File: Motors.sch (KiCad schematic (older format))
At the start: 12 parts

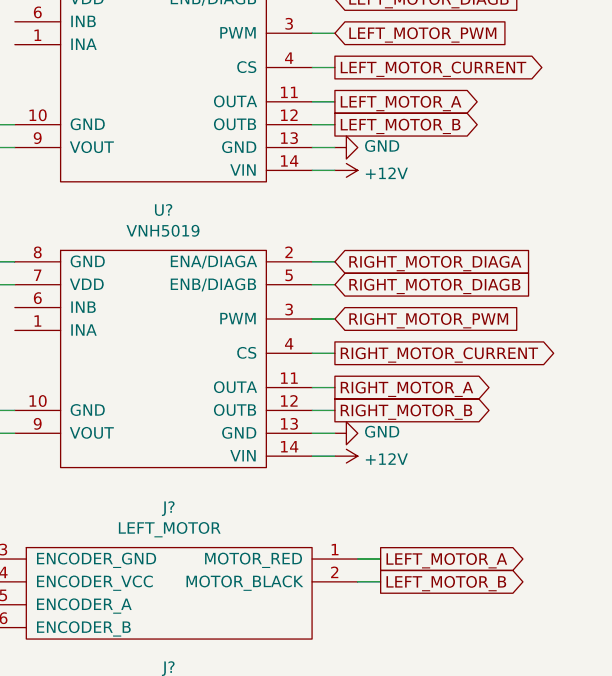
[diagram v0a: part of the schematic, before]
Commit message: Added fuses
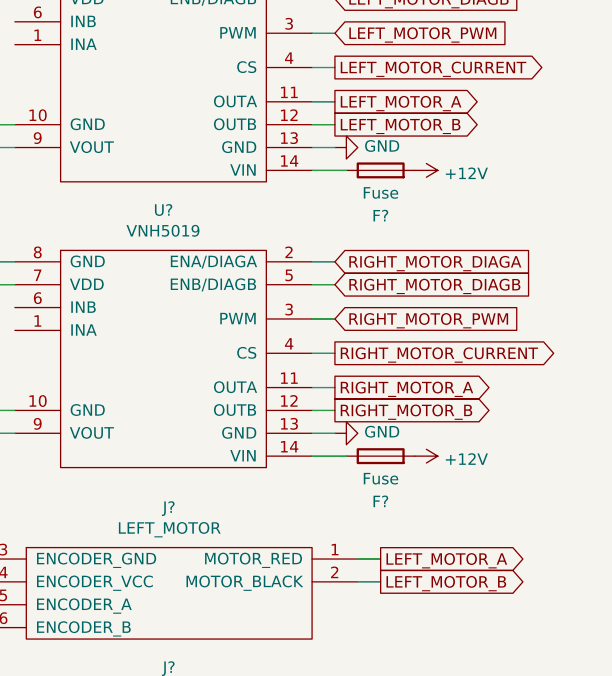
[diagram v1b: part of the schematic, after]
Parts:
- added F? (x2): Fuse, symbol Device:Fuse
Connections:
- net +12V: now also F?.2, F?.2; no longer U?.14 (VIN), U?.14 (VIN)
- new net: F?.1, U?.14 (VIN) (x2)
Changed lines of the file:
@@
 	6900 2300 7000 2300
-Wire Wire Line
-	6900 2400 7000 2400
 Wire Wire Line
 	5600 1550 5500 1550
@@
 L power:+12V #PWR?
 U 1 1 5E0DA565
-P 7000 3650
+P 7350 3650
 AR Path="/5E0DA565" Ref="#PWR?"  Part="1"
 AR Path="/5E0C61A9/5E0DA565" Ref="#PWR?"  Part="1"
-F 0 "#PWR?" H 7000 3500 50  0001 C CNN
-F 1 "+12V" V 7015 3778 50  0000 L CNN
-F 2 "" H 7000 3650 50  0001 C CNN
-F 3 "" H 7000 3650 50  0001 C CNN
-	1    7000 3650
+F 0 "#PWR?" H 7350 3500 50  0001 C CNN
+F 1 "+12V" V 7365 3778 50  0000 L CNN
+F 2 "" H 7350 3650 50  0001 C CNN
+F 3 "" H 7350 3650 50  0001 C CNN
+	1    7350 3650
 	0    1    1    0
 $EndComp
@@
 	6900 3550 7000 3550
 Wire Wire Line
-	6900 3650 7000 3650
-Wire Wire Line
 	5600 2800 5500 2800
 Wire Wire Line
@@
 L power:+12V #PWR?
 U 1 1 5E0DA62B
-P 7000 2400
+P 7350 2400
 AR Path="/5E0DA62B" Ref="#PWR?"  Part="1"
 AR Path="/5E0C61A9/5E0DA62B" Ref="#PWR?"  Part="1"
-F 0 "#PWR?" H 7000 2250 50  0001 C CNN
-F 1 "+12V" V 7015 2528 50  0000 L CNN
-F 2 "" H 7000 2400 50  0001 C CNN
-F 3 "" H 7000 2400 50  0001 C CNN
-	1    7000 2400
-	0    1    1    0
-$EndComp
+F 0 "#PWR?" H 7350 2250 50  0001 C CNN
+F 1 "+12V" V 7365 2528 50  0000 L CNN
+F 2 "" H 7350 2400 50  0001 C CNN
+F 3 "" H 7350 2400 50  0001 C CNN
+	1    7350 2400
+	0    1    1    0
+$EndComp
+$Comp
+L Device:Fuse F?
+U 1 1 5E2BC2E8
+P 7200 3650
+F 0 "F?" V 7000 3650 50  0000 C CNN
+F 1 "Fuse" V 7100 3650 50  0000 C CNN
+F 2 "" V 7130 3650 50  0001 C CNN
+F 3 "~" H 7200 3650 50  0001 C CNN
+	1    7200 3650
+	0    -1   -1   0
+$EndComp
+Wire Wire Line
+	6900 3650 7050 3650
+$Comp
+L Device:Fuse F?
+U 1 1 5E2BEBB4
+P 7200 2400
+F 0 "F?" V 7000 2400 50  0000 C CNN
+F 1 "Fuse" V 7100 2400 50  0000 C CNN
+F 2 "" V 7130 2400 50  0001 C CNN
+F 3 "~" H 7200 2400 50  0001 C CNN
+	1    7200 2400
+	0    -1   -1   0
+$EndComp
+Wire Wire Line
+	6900 2400 7050 2400
 $EndSCHEMATC

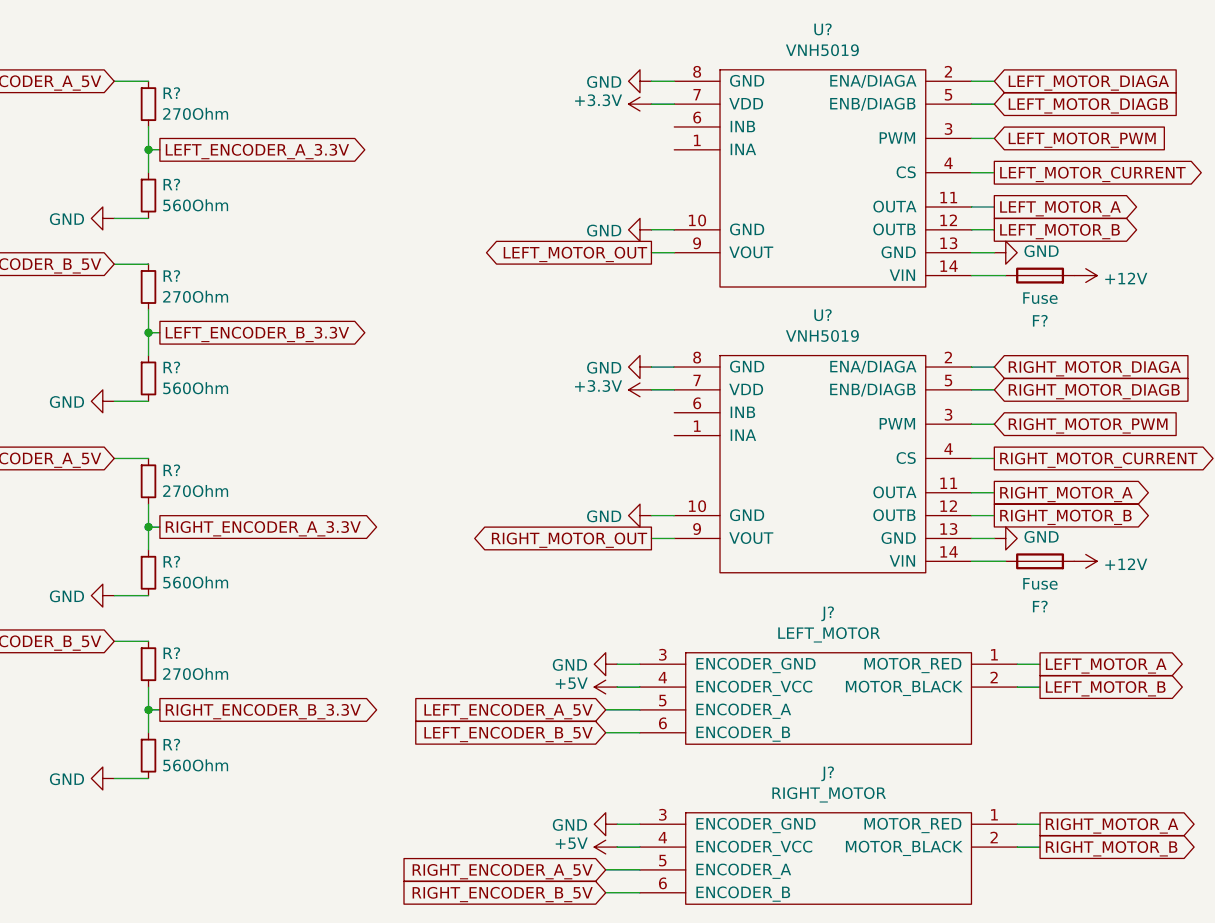
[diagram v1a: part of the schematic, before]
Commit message: Added footprints
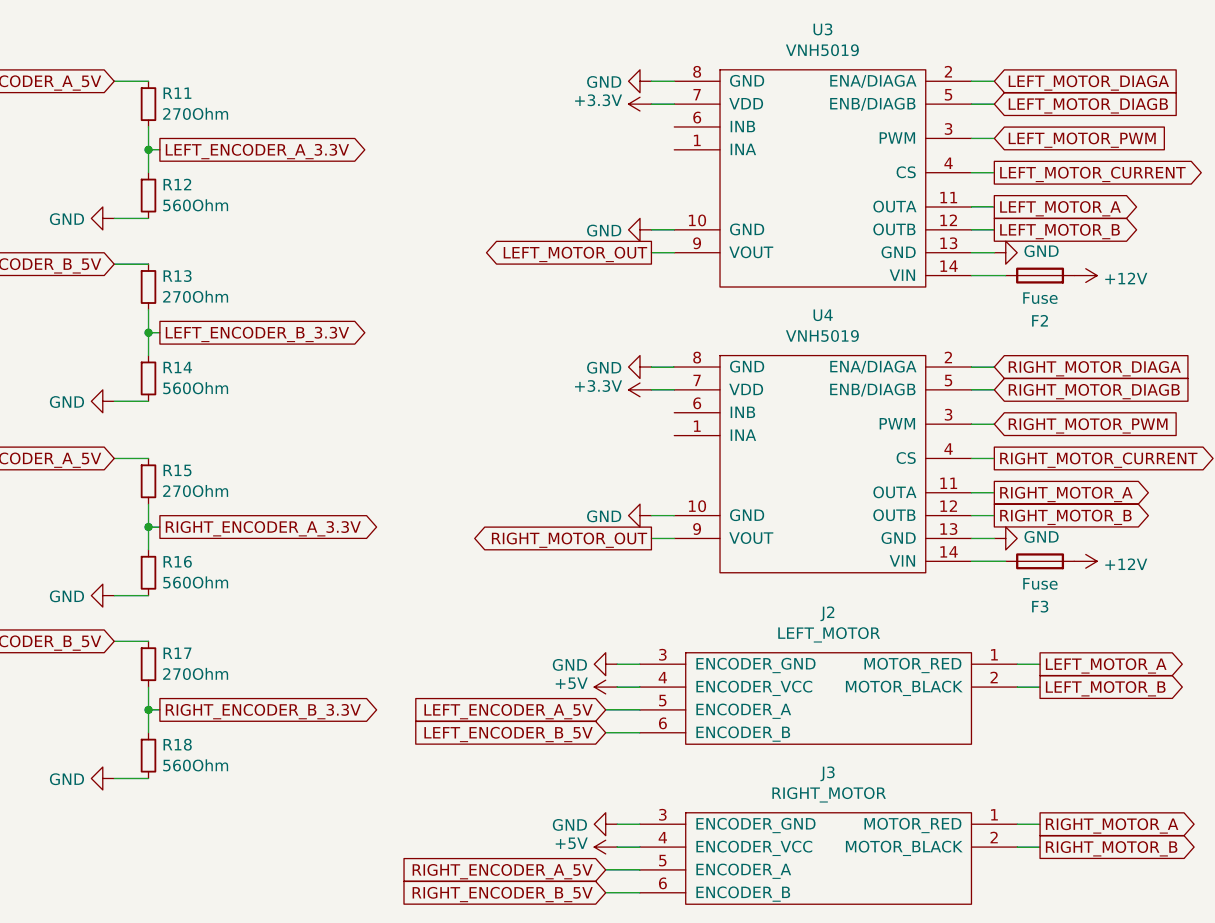
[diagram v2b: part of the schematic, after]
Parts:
- gave numbers to parts that had none: 14
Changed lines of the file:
@@
 P 6200 2500
 AR Path="/5E0DA51C" Ref="U?"  Part="1"
-AR Path="/5E0C61A9/5E0DA51C" Ref="U?"  Part="1"
-F 0 "U?" H 6250 3675 50  0000 C CNN
+AR Path="/5E0C61A9/5E0DA51C" Ref="U3"  Part="1"
+F 0 "U3" H 6250 3675 50  0000 C CNN
 F 1 "VNH5019" H 6250 3584 50  0000 C CNN
 F 2 "" H 6200 2500 50  0001 C CNN
@@
 P 5500 1550
 AR Path="/5E0DA522" Ref="#PWR?"  Part="1"
-AR Path="/5E0C61A9/5E0DA522" Ref="#PWR?"  Part="1"
-F 0 "#PWR?" H 5500 1300 50  0001 C CNN
+AR Path="/5E0C61A9/5E0DA522" Ref="#PWR0131"  Part="1"
+F 0 "#PWR0131" H 5500 1300 50  0001 C CNN
 F 1 "GND" V 5505 1422 50  0000 R CNN
 F 2 "" H 5500 1550 50  0001 C CNN
@@
 P 5500 2200
 AR Path="/5E0DA528" Ref="#PWR?"  Part="1"
-AR Path="/5E0C61A9/5E0DA528" Ref="#PWR?"  Part="1"
-F 0 "#PWR?" H 5500 1950 50  0001 C CNN
+AR Path="/5E0C61A9/5E0DA528" Ref="#PWR0132"  Part="1"
+F 0 "#PWR0132" H 5500 1950 50  0001 C CNN
 F 1 "GND" V 5505 2072 50  0000 R CNN
 F 2 "" H 5500 2200 50  0001 C CNN
@@
 P 5500 1650
 AR Path="/5E0DA52E" Ref="#PWR?"  Part="1"
-AR Path="/5E0C61A9/5E0DA52E" Ref="#PWR?"  Part="1"
-F 0 "#PWR?" H 5500 1500 50  0001 C CNN
+AR Path="/5E0C61A9/5E0DA52E" Ref="#PWR0133"  Part="1"
+F 0 "#PWR0133" H 5500 1500 50  0001 C CNN
 F 1 "+3.3V" V 5515 1778 50  0000 L CNN
 F 2 "" H 5500 1650 50  0001 C CNN
@@
 P 7000 2300
 AR Path="/5E0DA534" Ref="#PWR?"  Part="1"
-AR Path="/5E0C61A9/5E0DA534" Ref="#PWR?"  Part="1"
-F 0 "#PWR?" H 7000 2050 50  0001 C CNN
+AR Path="/5E0C61A9/5E0DA534" Ref="#PWR0134"  Part="1"
+F 0 "#PWR0134" H 7000 2050 50  0001 C CNN
 F 1 "GND" V 7005 2172 50  0000 R CNN
 F 2 "" H 7000 2300 50  0001 C CNN
@@
 P 6200 3750
 AR Path="/5E0DA54D" Ref="U?"  Part="1"
-AR Path="/5E0C61A9/5E0DA54D" Ref="U?"  Part="1"
-F 0 "U?" H 6250 4925 50  0000 C CNN
+AR Path="/5E0C61A9/5E0DA54D" Ref="U4"  Part="1"
+F 0 "U4" H 6250 4925 50  0000 C CNN
 F 1 "VNH5019" H 6250 4834 50  0000 C CNN
 F 2 "" H 6200 3750 50  0001 C CNN
@@
 P 5500 2800
 AR Path="/5E0DA553" Ref="#PWR?"  Part="1"
-AR Path="/5E0C61A9/5E0DA553" Ref="#PWR?"  Part="1"
-F 0 "#PWR?" H 5500 2550 50  0001 C CNN
+AR Path="/5E0C61A9/5E0DA553" Ref="#PWR0135"  Part="1"
+F 0 "#PWR0135" H 5500 2550 50  0001 C CNN
 F 1 "GND" V 5505 2672 50  0000 R CNN
 F 2 "" H 5500 2800 50  0001 C CNN
@@
 P 5500 3450
 AR Path="/5E0DA559" Ref="#PWR?"  Part="1"
-AR Path="/5E0C61A9/5E0DA559" Ref="#PWR?"  Part="1"
-F 0 "#PWR?" H 5500 3200 50  0001 C CNN
+AR Path="/5E0C61A9/5E0DA559" Ref="#PWR0136"  Part="1"
+F 0 "#PWR0136" H 5500 3200 50  0001 C CNN
 F 1 "GND" V 5505 3322 50  0000 R CNN
 F 2 "" H 5500 3450 50  0001 C CNN
@@
 P 5500 2900
 AR Path="/5E0DA55F" Ref="#PWR?"  Part="1"
-AR Path="/5E0C61A9/5E0DA55F" Ref="#PWR?"  Part="1"
-F 0 "#PWR?" H 5500 2750 50  0001 C CNN
+AR Path="/5E0C61A9/5E0DA55F" Ref="#PWR0137"  Part="1"
+F 0 "#PWR0137" H 5500 2750 50  0001 C CNN
 F 1 "+3.3V" V 5515 3028 50  0000 L CNN
 F 2 "" H 5500 2900 50  0001 C CNN
@@
 P 7350 3650
 AR Path="/5E0DA565" Ref="#PWR?"  Part="1"
-AR Path="/5E0C61A9/5E0DA565" Ref="#PWR?"  Part="1"
-F 0 "#PWR?" H 7350 3500 50  0001 C CNN
+AR Path="/5E0C61A9/5E0DA565" Ref="#PWR0138"  Part="1"
+F 0 "#PWR0138" H 7350 3500 50  0001 C CNN
 F 1 "+12V" V 7365 3778 50  0000 L CNN
 F 2 "" H 7350 3650 50  0001 C CNN
@@
 P 7000 3550
 AR Path="/5E0DA56B" Ref="#PWR?"  Part="1"
-AR Path="/5E0C61A9/5E0DA56B" Ref="#PWR?"  Part="1"
-F 0 "#PWR?" H 7000 3300 50  0001 C CNN
+AR Path="/5E0C61A9/5E0DA56B" Ref="#PWR0139"  Part="1"
+F 0 "#PWR0139" H 7000 3300 50  0001 C CNN
 F 1 "GND" V 7005 3422 50  0000 R CNN
 F 2 "" H 7000 3550 50  0001 C CNN
@@
 P 6300 4550
 AR Path="/5E0DA584" Ref="J?"  Part="1"
-AR Path="/5E0C61A9/5E0DA584" Ref="J?"  Part="1"
-F 0 "J?" H 6275 5225 50  0000 C CNN
+AR Path="/5E0C61A9/5E0DA584" Ref="J2"  Part="1"
+F 0 "J2" H 6275 5225 50  0000 C CNN
 F 1 "LEFT_MOTOR" H 6275 5134 50  0000 C CNN
 F 2 "" H 6300 4550 50  0001 C CNN
@@
 P 6300 5250
 AR Path="/5E0DA58A" Ref="J?"  Part="1"
-AR Path="/5E0C61A9/5E0DA58A" Ref="J?"  Part="1"
-F 0 "J?" H 6275 5925 50  0000 C CNN
+AR Path="/5E0C61A9/5E0DA58A" Ref="J3"  Part="1"
+F 0 "J3" H 6275 5925 50  0000 C CNN
 F 1 "RIGHT_MOTOR" H 6275 5834 50  0000 C CNN
 F 2 "" H 6300 5250 50  0001 C CNN
@@
 P 5350 4100
 AR Path="/5E0DA594" Ref="#PWR?"  Part="1"
-AR Path="/5E0C61A9/5E0DA594" Ref="#PWR?"  Part="1"
-F 0 "#PWR?" H 5350 3850 50  0001 C CNN
+AR Path="/5E0C61A9/5E0DA594" Ref="#PWR0140"  Part="1"
+F 0 "#PWR0140" H 5350 3850 50  0001 C CNN
 F 1 "GND" V 5355 3972 50  0000 R CNN
 F 2 "" H 5350 4100 50  0001 C CNN
@@
 P 5350 4800
 AR Path="/5E0DA59A" Ref="#PWR?"  Part="1"
-AR Path="/5E0C61A9/5E0DA59A" Ref="#PWR?"  Part="1"
-F 0 "#PWR?" H 5350 4550 50  0001 C CNN
+AR Path="/5E0C61A9/5E0DA59A" Ref="#PWR0141"  Part="1"
+F 0 "#PWR0141" H 5350 4550 50  0001 C CNN
 F 1 "GND" V 5355 4672 50  0000 R CNN
 F 2 "" H 5350 4800 50  0001 C CNN
@@
 P 5350 4200
 AR Path="/5E0DA5A0" Ref="#PWR?"  Part="1"
-AR Path="/5E0C61A9/5E0DA5A0" Ref="#PWR?"  Part="1"
-F 0 "#PWR?" H 5350 4050 50  0001 C CNN
+AR Path="/5E0C61A9/5E0DA5A0" Ref="#PWR0142"  Part="1"
+F 0 "#PWR0142" H 5350 4050 50  0001 C CNN
 F 1 "+5V" V 5365 4328 50  0000 L CNN
 F 2 "" H 5350 4200 50  0001 C CNN
@@
 P 5350 4900
 AR Path="/5E0DA5A6" Ref="#PWR?"  Part="1"
-AR Path="/5E0C61A9/5E0DA5A6" Ref="#PWR?"  Part="1"
-F 0 "#PWR?" H 5350 4750 50  0001 C CNN
+AR Path="/5E0C61A9/5E0DA5A6" Ref="#PWR0143"  Part="1"
+F 0 "#PWR0143" H 5350 4750 50  0001 C CNN
 F 1 "+5V" V 5365 5028 50  0000 L CNN
 F 2 "" H 5350 4900 50  0001 C CNN
@@
 P 3300 1650
 AR Path="/5E0DA5BD" Ref="R?"  Part="1"
-AR Path="/5E0C61A9/5E0DA5BD" Ref="R?"  Part="1"
-F 0 "R?" H 3359 1696 50  0000 L CNN
+AR Path="/5E0C61A9/5E0DA5BD" Ref="R11"  Part="1"
+F 0 "R11" H 3359 1696 50  0000 L CNN
 F 1 "270Ohm" H 3359 1605 50  0000 L CNN
 F 2 "" H 3300 1650 50  0001 C CNN
@@
 P 3300 2050
 AR Path="/5E0DA5C3" Ref="R?"  Part="1"
-AR Path="/5E0C61A9/5E0DA5C3" Ref="R?"  Part="1"
-F 0 "R?" H 3359 2096 50  0000 L CNN
+AR Path="/5E0C61A9/5E0DA5C3" Ref="R12"  Part="1"
+F 0 "R12" H 3359 2096 50  0000 L CNN
 F 1 "560Ohm" H 3359 2005 50  0000 L CNN
 F 2 "" H 3300 2050 50  0001 C CNN
@@
 P 3150 2150
 AR Path="/5E0DA5C9" Ref="#PWR?"  Part="1"
-AR Path="/5E0C61A9/5E0DA5C9" Ref="#PWR?"  Part="1"
-F 0 "#PWR?" H 3150 1900 50  0001 C CNN
+AR Path="/5E0C61A9/5E0DA5C9" Ref="#PWR0144"  Part="1"
+F 0 "#PWR0144" H 3150 1900 50  0001 C CNN
 F 1 "GND" V 3155 2022 50  0000 R CNN
 F 2 "" H 3150 2150 50  0001 C CNN
@@
 P 3300 2450
 AR Path="/5E0DA5D7" Ref="R?"  Part="1"
-AR Path="/5E0C61A9/5E0DA5D7" Ref="R?"  Part="1"
-F 0 "R?" H 3359 2496 50  0000 L CNN
+AR Path="/5E0C61A9/5E0DA5D7" Ref="R13"  Part="1"
+F 0 "R13" H 3359 2496 50  0000 L CNN
 F 1 "270Ohm" H 3359 2405 50  0000 L CNN
 F 2 "" H 3300 2450 50  0001 C CNN
@@
 P 3300 2850
 AR Path="/5E0DA5DD" Ref="R?"  Part="1"
-AR Path="/5E0C61A9/5E0DA5DD" Ref="R?"  Part="1"
-F 0 "R?" H 3359 2896 50  0000 L CNN
+AR Path="/5E0C61A9/5E0DA5DD" Ref="R14"  Part="1"
+F 0 "R14" H 3359 2896 50  0000 L CNN
 F 1 "560Ohm" H 3359 2805 50  0000 L CNN
 F 2 "" H 3300 2850 50  0001 C CNN
@@
 P 3150 2950
 AR Path="/5E0DA5E3" Ref="#PWR?"  Part="1"
-AR Path="/5E0C61A9/5E0DA5E3" Ref="#PWR?"  Part="1"
-F 0 "#PWR?" H 3150 2700 50  0001 C CNN
+AR Path="/5E0C61A9/5E0DA5E3" Ref="#PWR0145"  Part="1"
+F 0 "#PWR0145" H 3150 2700 50  0001 C CNN
 F 1 "GND" V 3155 2822 50  0000 R CNN
 F 2 "" H 3150 2950 50  0001 C CNN
@@
 P 3300 3300
 AR Path="/5E0DA5F1" Ref="R?"  Part="1"
-AR Path="/5E0C61A9/5E0DA5F1" Ref="R?"  Part="1"
-F 0 "R?" H 3359 3346 50  0000 L CNN
+AR Path="/5E0C61A9/5E0DA5F1" Ref="R15"  Part="1"
+F 0 "R15" H 3359 3346 50  0000 L CNN
 F 1 "270Ohm" H 3359 3255 50  0000 L CNN
 F 2 "" H 3300 3300 50  0001 C CNN
@@
 P 3300 3700
 AR Path="/5E0DA5F7" Ref="R?"  Part="1"
-AR Path="/5E0C61A9/5E0DA5F7" Ref="R?"  Part="1"
-F 0 "R?" H 3359 3746 50  0000 L CNN
+AR Path="/5E0C61A9/5E0DA5F7" Ref="R16"  Part="1"
+F 0 "R16" H 3359 3746 50  0000 L CNN
 F 1 "560Ohm" H 3359 3655 50  0000 L CNN
 F 2 "" H 3300 3700 50  0001 C CNN
@@
 P 3150 3800
 AR Path="/5E0DA5FD" Ref="#PWR?"  Part="1"
-AR Path="/5E0C61A9/5E0DA5FD" Ref="#PWR?"  Part="1"
-F 0 "#PWR?" H 3150 3550 50  0001 C CNN
+AR Path="/5E0C61A9/5E0DA5FD" Ref="#PWR0146"  Part="1"
+F 0 "#PWR0146" H 3150 3550 50  0001 C CNN
 F 1 "GND" V 3155 3672 50  0000 R CNN
 F 2 "" H 3150 3800 50  0001 C CNN
@@
 P 3300 4100
 AR Path="/5E0DA60B" Ref="R?"  Part="1"
-AR Path="/5E0C61A9/5E0DA60B" Ref="R?"  Part="1"
-F 0 "R?" H 3359 4146 50  0000 L CNN
+AR Path="/5E0C61A9/5E0DA60B" Ref="R17"  Part="1"
+F 0 "R17" H 3359 4146 50  0000 L CNN
 F 1 "270Ohm" H 3359 4055 50  0000 L CNN
 F 2 "" H 3300 4100 50  0001 C CNN
@@
 P 3300 4500
 AR Path="/5E0DA611" Ref="R?"  Part="1"
-AR Path="/5E0C61A9/5E0DA611" Ref="R?"  Part="1"
-F 0 "R?" H 3359 4546 50  0000 L CNN
+AR Path="/5E0C61A9/5E0DA611" Ref="R18"  Part="1"
+F 0 "R18" H 3359 4546 50  0000 L CNN
 F 1 "560Ohm" H 3359 4455 50  0000 L CNN
 F 2 "" H 3300 4500 50  0001 C CNN
@@
 P 3150 4600
 AR Path="/5E0DA617" Ref="#PWR?"  Part="1"
-AR Path="/5E0C61A9/5E0DA617" Ref="#PWR?"  Part="1"
-F 0 "#PWR?" H 3150 4350 50  0001 C CNN
+AR Path="/5E0C61A9/5E0DA617" Ref="#PWR0147"  Part="1"
+F 0 "#PWR0147" H 3150 4350 50  0001 C CNN
 F 1 "GND" V 3155 4472 50  0000 R CNN
 F 2 "" H 3150 4600 50  0001 C CNN
@@
 P 7350 2400
 AR Path="/5E0DA62B" Ref="#PWR?"  Part="1"
-AR Path="/5E0C61A9/5E0DA62B" Ref="#PWR?"  Part="1"
-F 0 "#PWR?" H 7350 2250 50  0001 C CNN
+AR Path="/5E0C61A9/5E0DA62B" Ref="#PWR0148"  Part="1"
+F 0 "#PWR0148" H 7350 2250 50  0001 C CNN
 F 1 "+12V" V 7365 2528 50  0000 L CNN
 F 2 "" H 7350 2400 50  0001 C CNN
@@
 $EndComp
 $Comp
-L Device:Fuse F?
+L Device:Fuse F3
 U 1 1 5E2BC2E8
 P 7200 3650
-F 0 "F?" V 7000 3650 50  0000 C CNN
+F 0 "F3" V 7000 3650 50  0000 C CNN
 F 1 "Fuse" V 7100 3650 50  0000 C CNN
 F 2 "" V 7130 3650 50  0001 C CNN
@@
 	6900 3650 7050 3650
 $Comp
-L Device:Fuse F?
+L Device:Fuse F2
 U 1 1 5E2BEBB4
 P 7200 2400
-F 0 "F?" V 7000 2400 50  0000 C CNN
+F 0 "F2" V 7000 2400 50  0000 C CNN
 F 1 "Fuse" V 7100 2400 50  0000 C CNN
 F 2 "" V 7130 2400 50  0001 C CNN

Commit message: Added footprints
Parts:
- F2, F3: footprint (none) -> Fuse:Fuse_0805_2012Metric_Pad1.15x1.40mm_HandSolder
- J2, J3: footprint (none) -> Connector_PinHeader_2.54mm:PinHeader_1x06_P2.54mm_Vertical
- R11, R12, R13, R14, R15, R16, R17, R18: footprint (none) -> Resistor_SMD:R_0603_1608Metric_Pad1.05x0.95mm_HandSolder
- U3, U4: footprint (none) -> TurtlebotController:Pololu_VNH5019_Carrier
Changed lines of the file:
@@
 F 0 "U3" H 6250 3675 50  0000 C CNN
 F 1 "VNH5019" H 6250 3584 50  0000 C CNN
-F 2 "" H 6200 2500 50  0001 C CNN
+F 2 "TurtlebotController:Pololu_VNH5019_Carrier" H 6200 2500 50  0001 C CNN
 F 3 "" H 6200 2500 50  0001 C CNN
 	1    6200 2500
@@
 F 0 "U4" H 6250 4925 50  0000 C CNN
 F 1 "VNH5019" H 6250 4834 50  0000 C CNN
-F 2 "" H 6200 3750 50  0001 C CNN
+F 2 "TurtlebotController:Pololu_VNH5019_Carrier" H 6200 3750 50  0001 C CNN
 F 3 "" H 6200 3750 50  0001 C CNN
 	1    6200 3750
@@
 F 0 "J2" H 6275 5225 50  0000 C CNN
 F 1 "LEFT_MOTOR" H 6275 5134 50  0000 C CNN
-F 2 "" H 6300 4550 50  0001 C CNN
+F 2 "Connector_PinHeader_2.54mm:PinHeader_1x06_P2.54mm_Vertical" H 6300 4550 50  0001 C CNN
 F 3 "" H 6300 4550 50  0001 C CNN
 	1    6300 4550
@@
 F 0 "J3" H 6275 5925 50  0000 C CNN
 F 1 "RIGHT_MOTOR" H 6275 5834 50  0000 C CNN
-F 2 "" H 6300 5250 50  0001 C CNN
+F 2 "Connector_PinHeader_2.54mm:PinHeader_1x06_P2.54mm_Vertical" H 6300 5250 50  0001 C CNN
 F 3 "" H 6300 5250 50  0001 C CNN
 	1    6300 5250
@@
 F 0 "R11" H 3359 1696 50  0000 L CNN
 F 1 "270Ohm" H 3359 1605 50  0000 L CNN
-F 2 "" H 3300 1650 50  0001 C CNN
+F 2 "Resistor_SMD:R_0603_1608Metric_Pad1.05x0.95mm_HandSolder" H 3300 1650 50  0001 C CNN
 F 3 "~" H 3300 1650 50  0001 C CNN
 	1    3300 1650
@@
 F 0 "R12" H 3359 2096 50  0000 L CNN
 F 1 "560Ohm" H 3359 2005 50  0000 L CNN
-F 2 "" H 3300 2050 50  0001 C CNN
+F 2 "Resistor_SMD:R_0603_1608Metric_Pad1.05x0.95mm_HandSolder" H 3300 2050 50  0001 C CNN
 F 3 "~" H 3300 2050 50  0001 C CNN
 	1    3300 2050
@@
 F 0 "R13" H 3359 2496 50  0000 L CNN
 F 1 "270Ohm" H 3359 2405 50  0000 L CNN
-F 2 "" H 3300 2450 50  0001 C CNN
+F 2 "Resistor_SMD:R_0603_1608Metric_Pad1.05x0.95mm_HandSolder" H 3300 2450 50  0001 C CNN
 F 3 "~" H 3300 2450 50  0001 C CNN
 	1    3300 2450
@@
 F 0 "R14" H 3359 2896 50  0000 L CNN
 F 1 "560Ohm" H 3359 2805 50  0000 L CNN
-F 2 "" H 3300 2850 50  0001 C CNN
+F 2 "Resistor_SMD:R_0603_1608Metric_Pad1.05x0.95mm_HandSolder" H 3300 2850 50  0001 C CNN
 F 3 "~" H 3300 2850 50  0001 C CNN
 	1    3300 2850
@@
 F 0 "R15" H 3359 3346 50  0000 L CNN
 F 1 "270Ohm" H 3359 3255 50  0000 L CNN
-F 2 "" H 3300 3300 50  0001 C CNN
+F 2 "Resistor_SMD:R_0603_1608Metric_Pad1.05x0.95mm_HandSolder" H 3300 3300 50  0001 C CNN
 F 3 "~" H 3300 3300 50  0001 C CNN
 	1    3300 3300
@@
 F 0 "R16" H 3359 3746 50  0000 L CNN
 F 1 "560Ohm" H 3359 3655 50  0000 L CNN
-F 2 "" H 3300 3700 50  0001 C CNN
+F 2 "Resistor_SMD:R_0603_1608Metric_Pad1.05x0.95mm_HandSolder" H 3300 3700 50  0001 C CNN
 F 3 "~" H 3300 3700 50  0001 C CNN
 	1    3300 3700
@@
 F 0 "R17" H 3359 4146 50  0000 L CNN
 F 1 "270Ohm" H 3359 4055 50  0000 L CNN
-F 2 "" H 3300 4100 50  0001 C CNN
+F 2 "Resistor_SMD:R_0603_1608Metric_Pad1.05x0.95mm_HandSolder" H 3300 4100 50  0001 C CNN
 F 3 "~" H 3300 4100 50  0001 C CNN
 	1    3300 4100
@@
 F 0 "R18" H 3359 4546 50  0000 L CNN
 F 1 "560Ohm" H 3359 4455 50  0000 L CNN
-F 2 "" H 3300 4500 50  0001 C CNN
+F 2 "Resistor_SMD:R_0603_1608Metric_Pad1.05x0.95mm_HandSolder" H 3300 4500 50  0001 C CNN
 F 3 "~" H 3300 4500 50  0001 C CNN
 	1    3300 4500
@@
 F 0 "F3" V 7000 3650 50  0000 C CNN
 F 1 "Fuse" V 7100 3650 50  0000 C CNN
-F 2 "" V 7130 3650 50  0001 C CNN
+F 2 "Fuse:Fuse_0805_2012Metric_Pad1.15x1.40mm_HandSolder" V 7130 3650 50  0001 C CNN
 F 3 "~" H 7200 3650 50  0001 C CNN
 	1    7200 3650
@@
 F 0 "F2" V 7000 2400 50  0000 C CNN
 F 1 "Fuse" V 7100 2400 50  0000 C CNN
-F 2 "" V 7130 2400 50  0001 C CNN
+F 2 "Fuse:Fuse_0805_2012Metric_Pad1.15x1.40mm_HandSolder" V 7130 2400 50  0001 C CNN
 F 3 "~" H 7200 2400 50  0001 C CNN
 	1    7200 2400
